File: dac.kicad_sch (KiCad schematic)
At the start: 57 parts, among them J9 DAC OUT, Q2 FMMT591, Q3 FMMT491, Q4 FMMT491, Q5 FMMT591, U1 CJC4334H, U9 OPA1612AxD

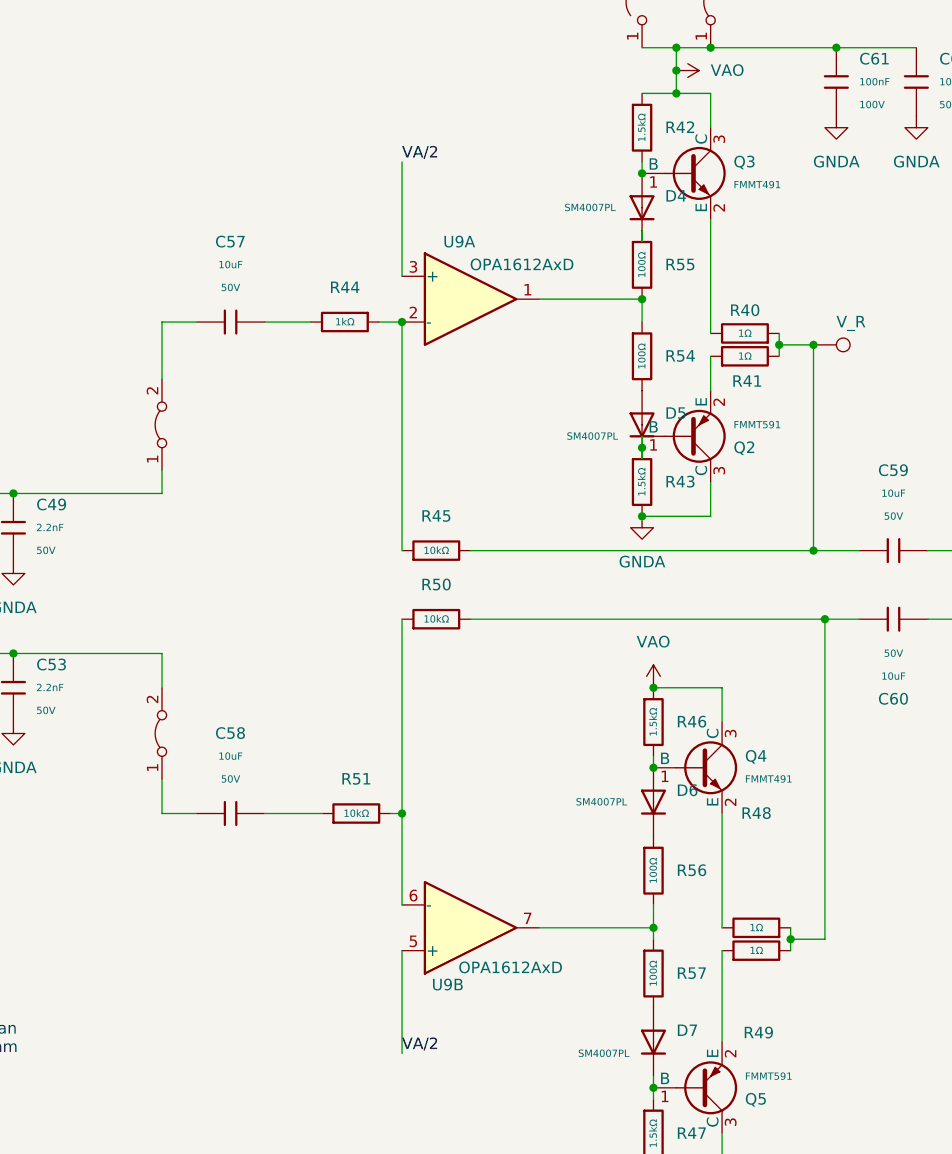
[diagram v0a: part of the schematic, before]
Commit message: Changed R55-58 values.
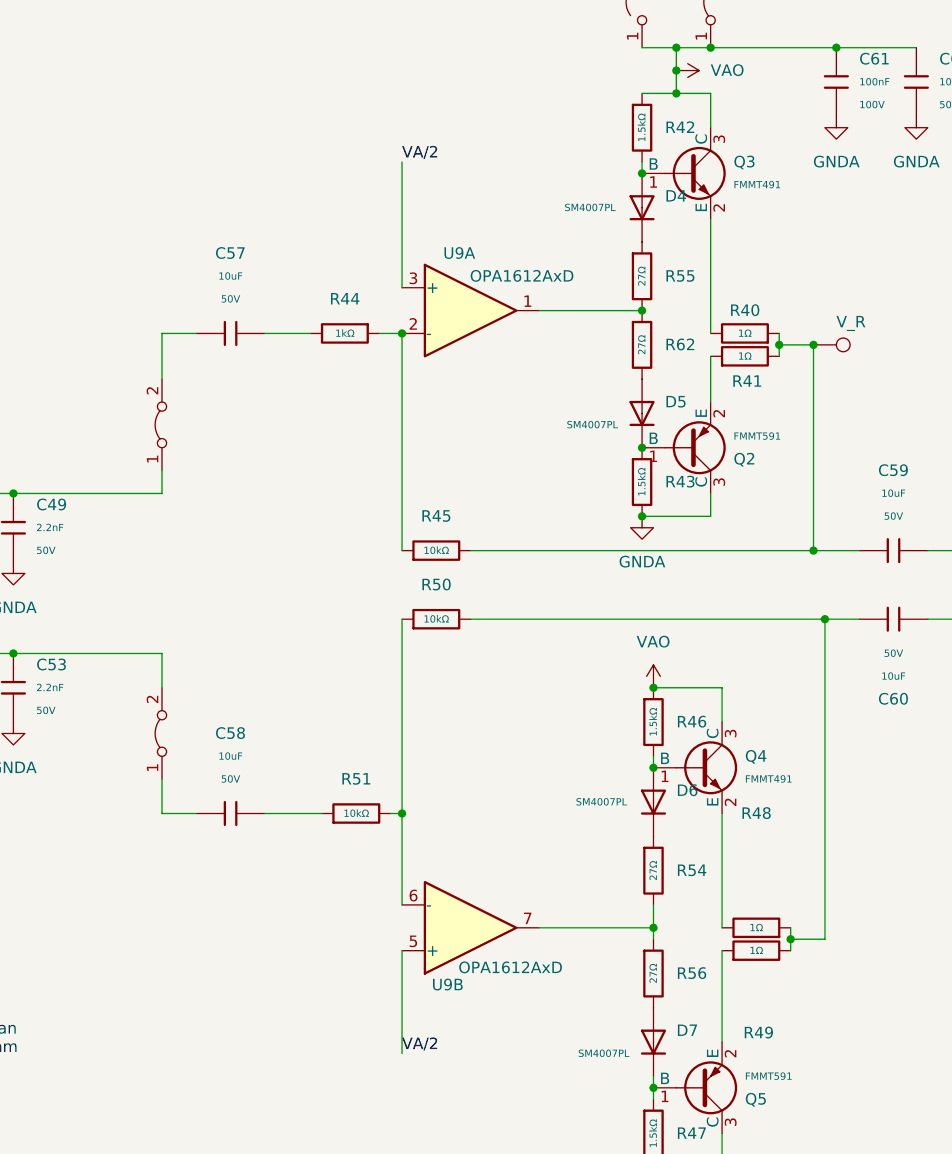
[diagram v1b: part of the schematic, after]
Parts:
- removed R54, R55, R56, R57: 100Ω, PCM_JLCPCB:R_0805, symbol PCM_JLCPCB-Resistors:0805,100Ω
- added R54, R55, R56, R62: 27Ω, PCM_JLCPCB:R_0805, symbol PCM_JLCPCB-Resistors:0805,27Ω
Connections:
- net at U9.7: now also R54.2, R56.1
- net at D7.2: now also R56.2
- net at U9.1: now also R55.2, R62.1
- net at D4.1: now also R55.1
- net at D6.1: now also R54.1
- net at D5.2: now also R62.2
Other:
- moved on the sheet: C57, D5, Q2, R44, U9A

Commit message: No Errors No Warnings
Some were excluded.
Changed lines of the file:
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@@
 	)
 	(hierarchical_label "MCLK"
-		(shape input)
+		(shape output)
 		(at 57.15 90.17 180)
 		(effects
@@
 	)
 	(hierarchical_label "LRCK"
-		(shape input)
+		(shape output)
 		(at 57.15 87.63 180)
 		(effects

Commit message: Beautifying it.
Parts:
- added C24, C25: 10uF, PCM_JLCPCB:C_0805, symbol PCM_JLCPCB-Capacitors:0805,10uF,(2)
- added C26: 100nF, PCM_JLCPCB:C_0805, symbol PCM_JLCPCB-Capacitors:0805,100nF
- added J16: DAC OUT LL, Intro_to_CAD:Jack_3.5mm_CUI_SJ-3523-SMT_Horizontal, symbol Connector_Audio:AudioJack2_Ground
- added R71: 10Ω, PCM_JLCPCB:R_0603, symbol PCM_JLCPCB-Resistors:0603,10Ω
- added e8: Groundloop_Insurance, Jumper:SolderJumper-2_P1.3mm_Bridged_RoundedPad1.0x1.5mm, symbol Jumper:Jumper_2_Bridged
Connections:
- net GNDA: now also C26.1, R71.2, e8.1 (A)
- net at C53.1, R33.2, e7.2 (B): now also C25.1
- net at C49.1, R22.2, e6.1 (A): now also C24.1
- new net: C26.2, J16.S, R71.1, e8.2 (B)
- new net: C24.2, J16.R
- new net: C25.2, J16.T

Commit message: Getting JLCPCB Price
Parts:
- J16: value DAC OUT LL -> DAC LL
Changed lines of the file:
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@@
 			)
 		)
-		(property "Value" "DAC OUT LL"
+		(property "Value" "DAC LL"
 			(at 144.018 83.312 0)
 			(effects

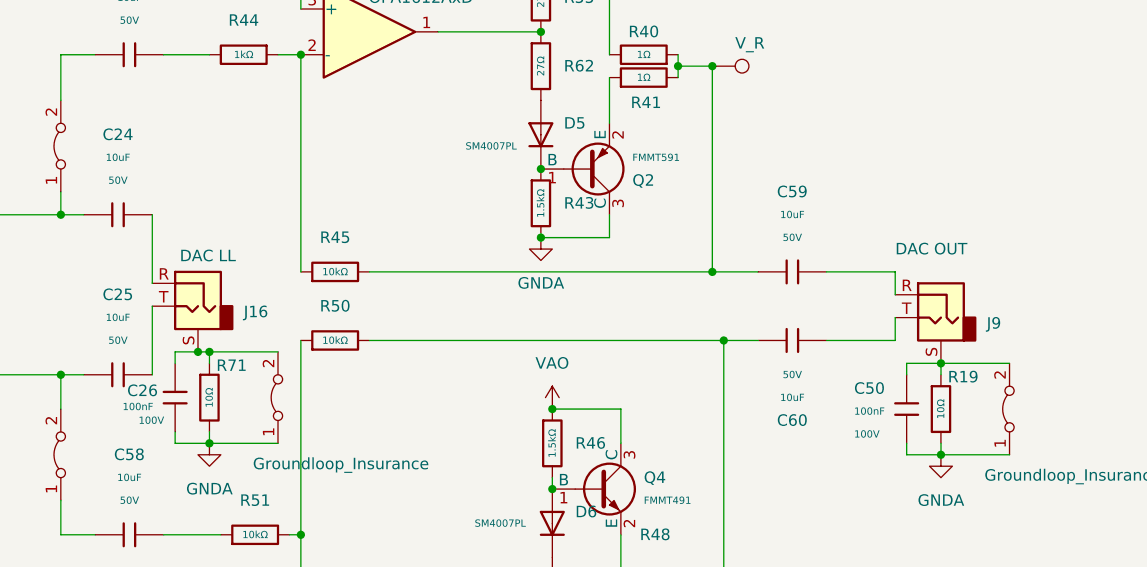
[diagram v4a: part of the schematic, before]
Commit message: Replaced Jaron's LEDs
They were only for Standard Boards.
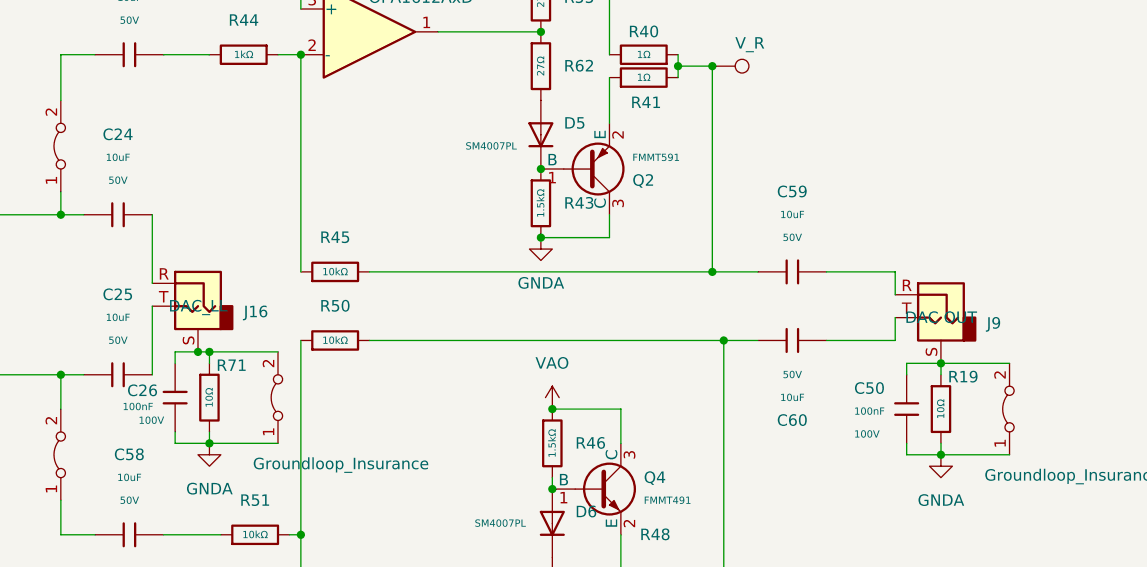
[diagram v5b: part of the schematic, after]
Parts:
- J16: value DAC LL -> 3.5mm_Jack
- J9: value DAC OUT -> 3.5mm_Jack
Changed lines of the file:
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@@
 			)
 		)
-		(property "Value" "DAC OUT"
+		(property "Value" "3.5mm_Jack"
 			(at 223.52 82.55 0)
 			(effects
@@
 				)
 				(justify right)
+				(hide yes)
 			)
 		)
@@
 			)
 		)
-		(property "Description" ""
+		(property "Description" "DAC OUT"
 			(at 228.6 90.17 0)
 			(effects
@@
 					(size 1.27 1.27)
 				)
-				(hide yes)
 			)
 		)
@@
 			)
 		)
-		(property "Value" "DAC LL"
+		(property "Value" "3.5mm_Jack"
 			(at 144.018 83.312 0)
 			(effects
@@
 				)
 				(justify right)
+				(hide yes)
 			)
 		)
@@
 			)
 		)
-		(property "Description" ""
+		(property "Description" "DAC_LL"
 			(at 146.05 88.9 0)
 			(effects
@@
 					(size 1.27 1.27)
 				)
-				(hide yes)
-			)
-		)
+			)
+		)

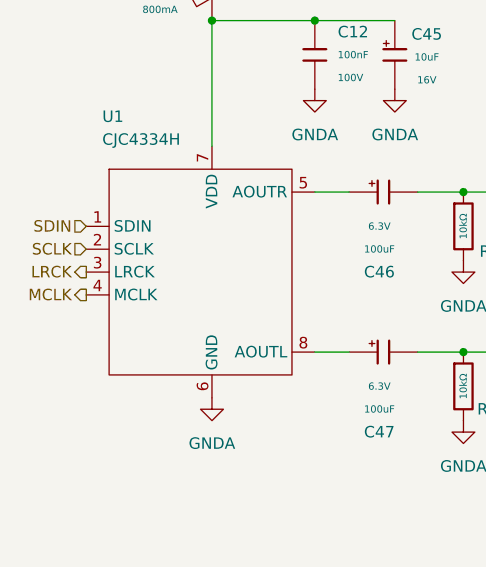
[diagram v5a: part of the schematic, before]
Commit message: Fixed DAC
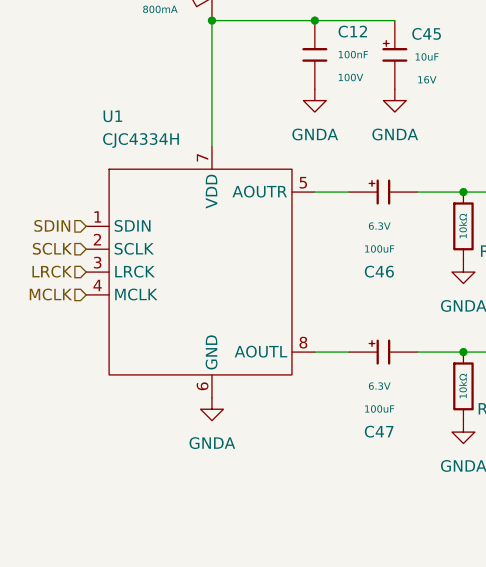
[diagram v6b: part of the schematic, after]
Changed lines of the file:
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@@
 	)
 	(hierarchical_label "MCLK"
-		(shape output)
+		(shape input)
 		(at 57.15 90.17 180)
 		(effects
@@
 	)
 	(hierarchical_label "LRCK"
-		(shape output)
+		(shape input)
 		(at 57.15 87.63 180)
 		(effects

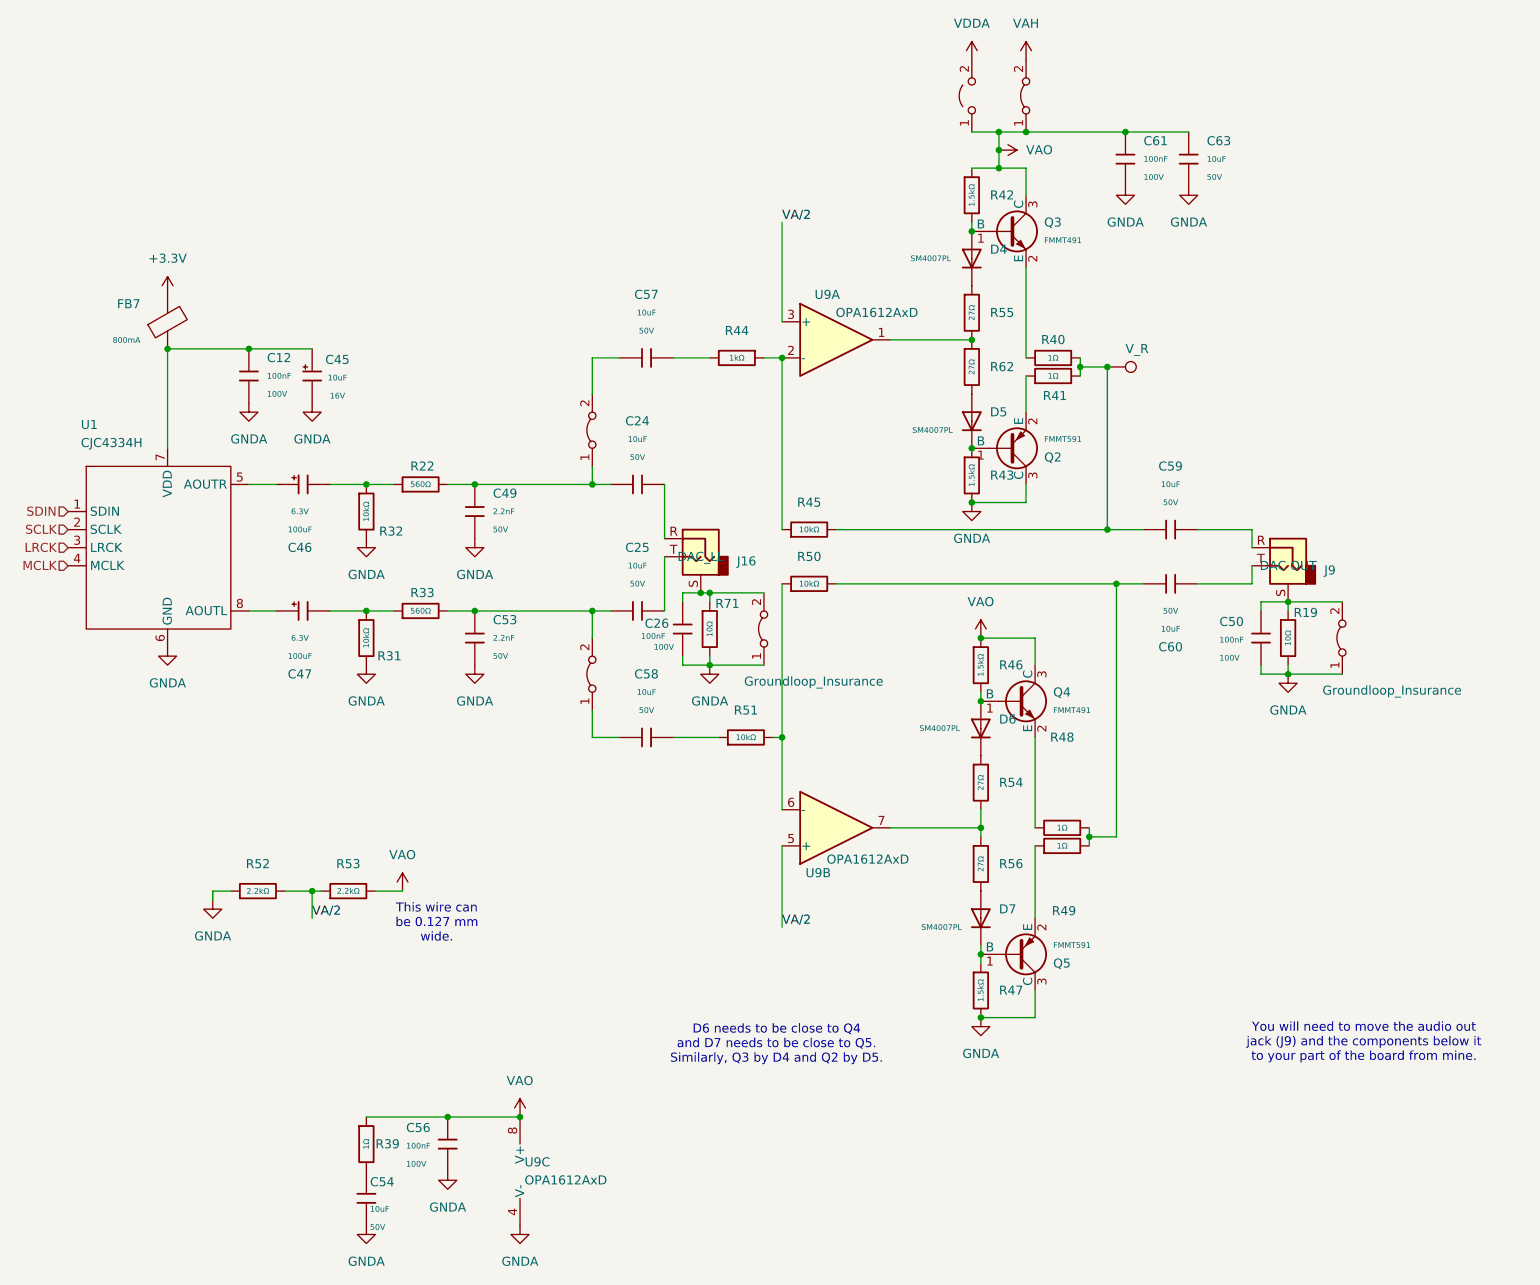
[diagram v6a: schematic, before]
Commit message: Fixed label on DAC schematic.
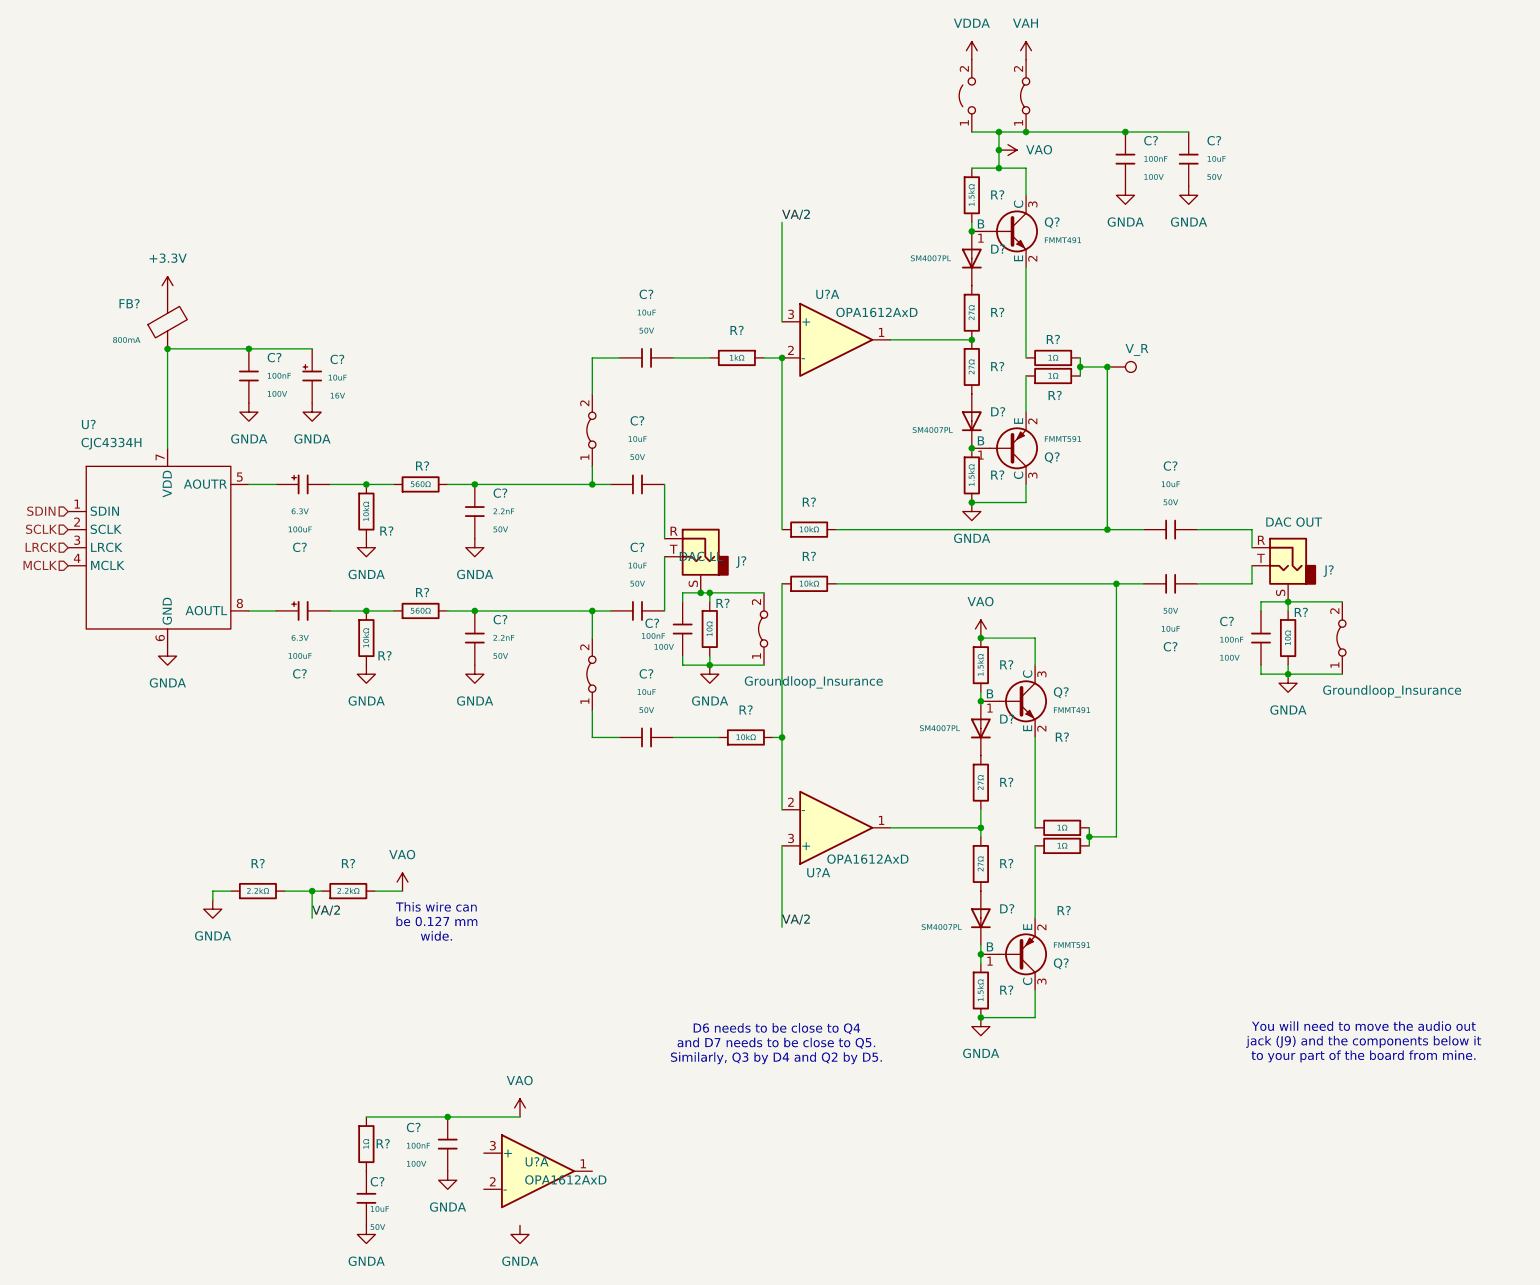
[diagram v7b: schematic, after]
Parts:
- renumbered C63 to C?, C26 to C?, C60 to C?, C50 to C?, C58 to C?, C24 to C?, C47 to C?, C53 to C?, C59 to C?, C56 to C?, C46 to C?, C54 to C?, C45 to C?, C57 to C?, C49 to C?, C61 to C?, C25 to C?, C12 to C?, D6 to D?, D7 to D?, D5 to D?, D4 to D?, FB7 to FB?, J9 to J?, J16 to J?, JP3 to JP?, Q2 to Q?, Q4 to Q?, Q5 to Q?, Q3 to Q?, R49 to R?, R44 to R?, R55 to R?, R43 to R?, R39 to R?, R33 to R?, R32 to R?, R31 to R?, R62 to R?, R47 to R?, R45 to R?, R71 to R?, R46 to R?, R56 to R?, R50 to R?, R40 to R?, R48 to R?, R42 to R?, R52 to R?, R51 to R?, R54 to R?, R22 to R?, R53 to R?, R19 to R?, R41 to R?, TP8 to TP?, U9 to U?, U1 to U?, e3 to e?, e7 to e?, e6 to e?, e8 to e?, e2 to e?
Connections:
- net GNDA: no longer U?.4 (V-)
- net VAO: no longer U?.8 (V+)
- net VA/2: now also U?.3 (+); no longer U?.5 (+)
- net at R?.1, R?.2: now also U?.1; no longer U?.7
- net at R?.1, R?.2: now also U?.2 (-); no longer U?.6 (-)
